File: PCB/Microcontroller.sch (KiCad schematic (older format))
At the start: 36 parts

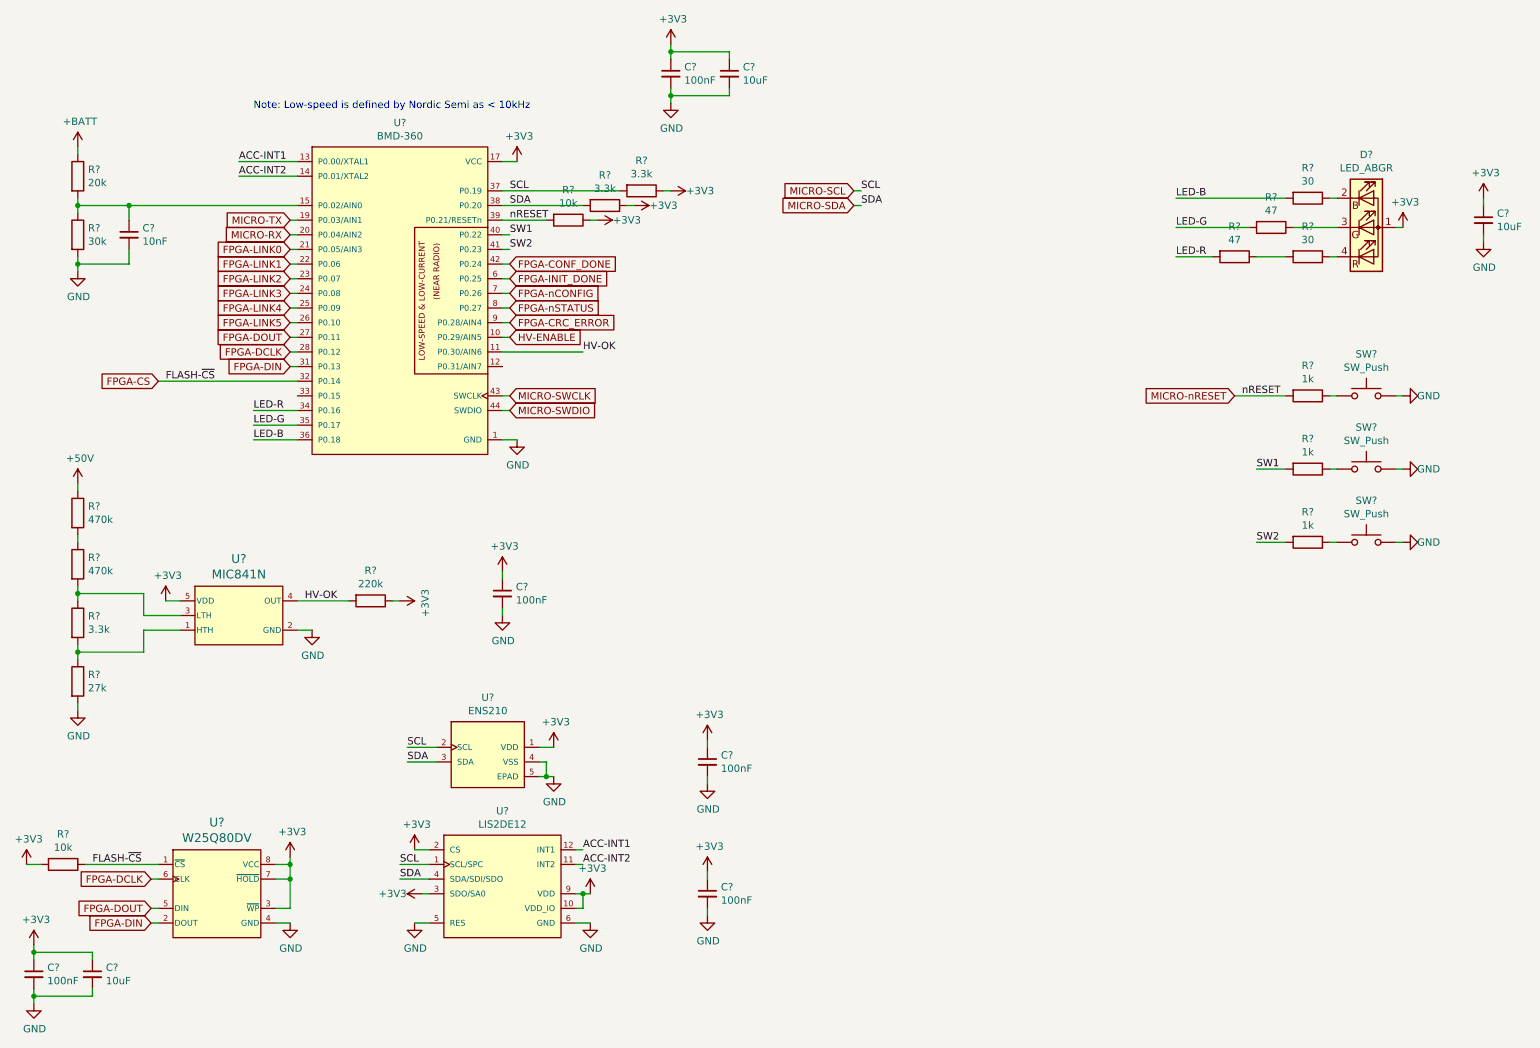
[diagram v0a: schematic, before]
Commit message: Annotate schematic, simplify transmit circuit, shuffle receive opamp stages, reorder buttons so they match net names, reorder connectors to simplify routing, begin arranging parts on PCB
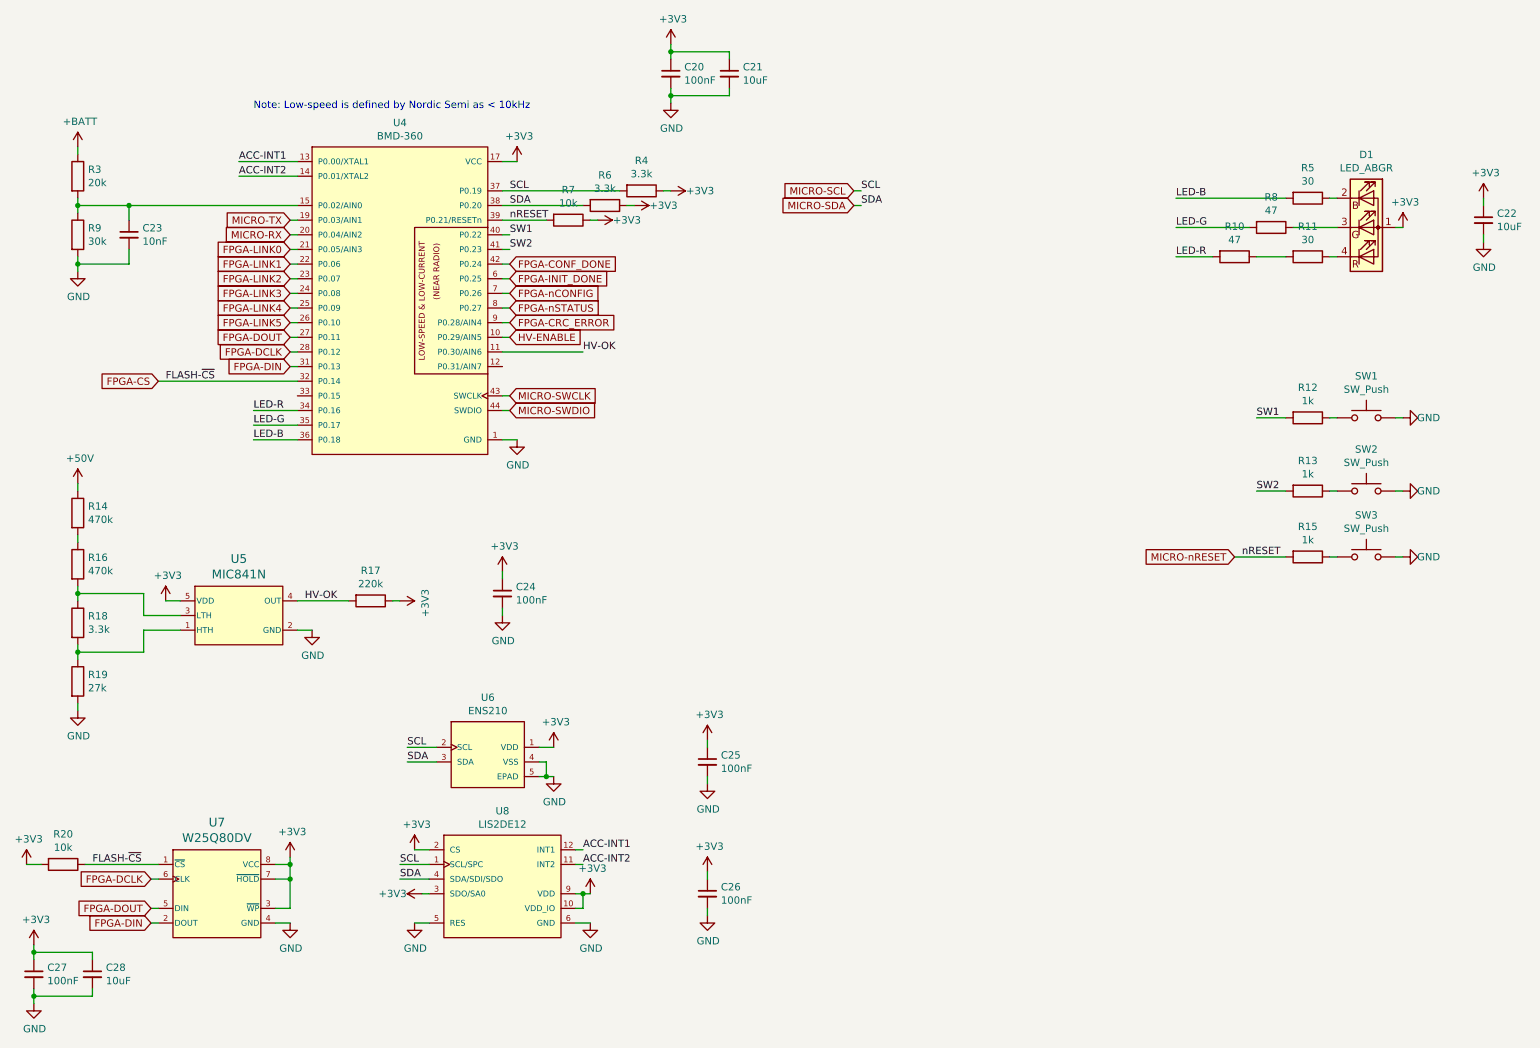
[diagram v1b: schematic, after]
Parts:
- gave numbers to parts that had none: 36
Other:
- moved on the sheet: R12, R13, R15, SW1, SW2, SW3

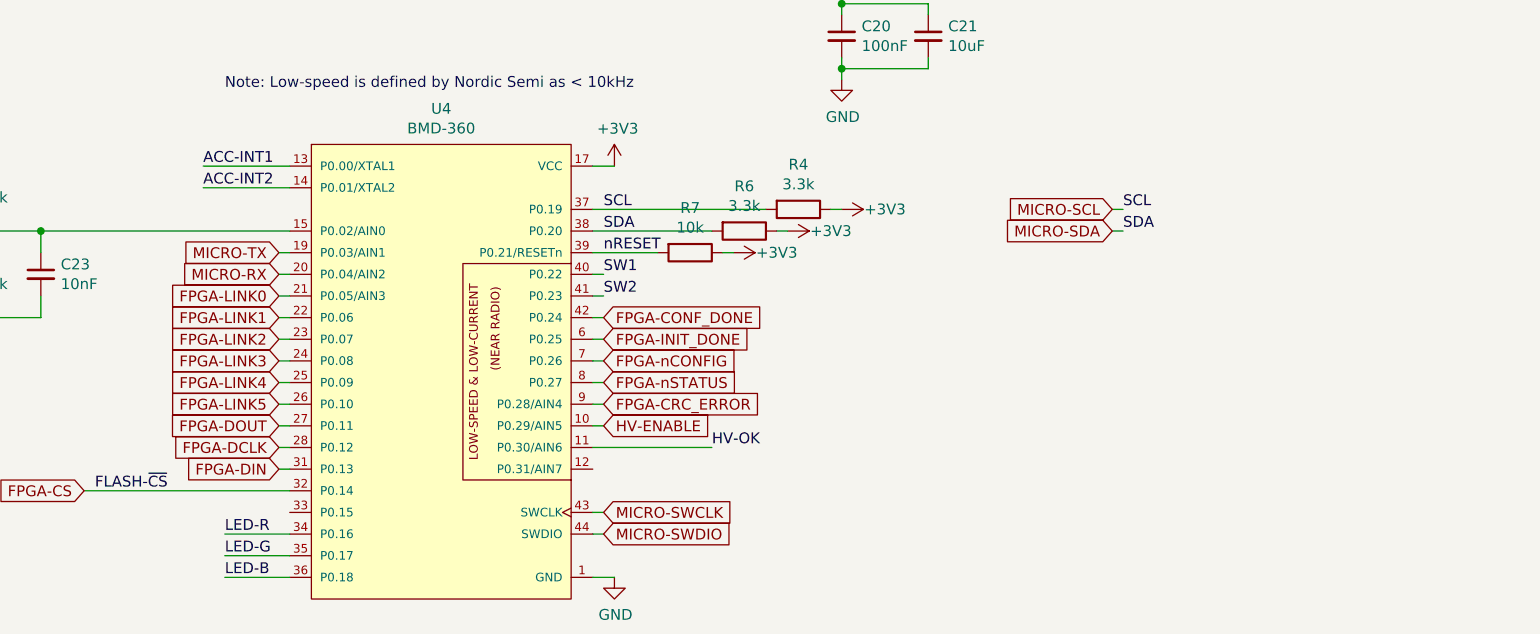
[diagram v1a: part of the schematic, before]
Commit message: Begin layout around FPGA and microcontroller, rearrange some connections to FPGA and microcontroller, change groupings of optional debug pins
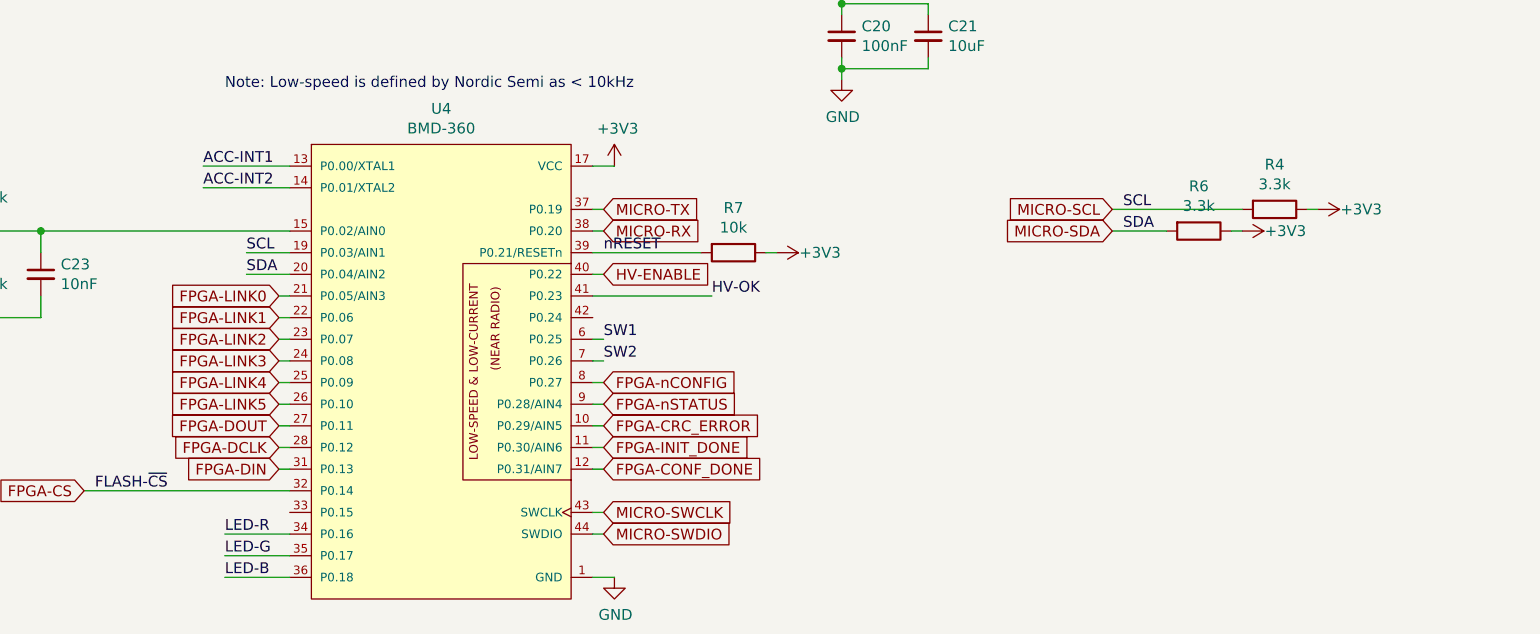
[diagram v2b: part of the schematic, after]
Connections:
- net FPGA-CONF_DONE: now also U4.12 (P0.31/AIN7); no longer U4.42 (P0.24)
- net FPGA-CRC_ERROR: now also U4.10 (P0.29/AIN5); no longer U4.9 (P0.28/AIN4)
- net FPGA-INIT_DONE: now also U4.11 (P0.30/AIN6); no longer U4.6 (P0.25)
- net FPGA-nCONFIG: now also U4.8 (P0.27); no longer U4.7 (P0.26)
- net FPGA-nSTATUS: now also U4.9 (P0.28/AIN4); no longer U4.8 (P0.27)
- net HV-ENABLE: now also U4.40 (P0.22); no longer U4.10 (P0.29/AIN5)
- net HV-OK: now also U4.41 (P0.23); no longer U4.11 (P0.30/AIN6)
- net MICRO-RX: now also U4.38 (P0.20); no longer U4.20 (P0.04/AIN2)
- net MICRO-SCL: now also U4.19 (P0.03/AIN1); no longer U4.37 (P0.19)
- net MICRO-SDA: now also U4.20 (P0.04/AIN2); no longer U4.38 (P0.20)
- net MICRO-TX: now also U4.37 (P0.19); no longer U4.19 (P0.03/AIN1)
- net SW1: now also U4.6 (P0.25); no longer U4.40 (P0.22)
- net SW2: now also U4.7 (P0.26); no longer U4.41 (P0.23)
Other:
- moved on the sheet: R4, R6, R7
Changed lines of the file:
@@
 	1    0    0    -1
 $EndComp
-Text GLabel 2500 2100 0    50   Input ~ 0
+Text GLabel 4000 1900 2    50   Input ~ 0
 MICRO-TX
-Text GLabel 2500 2200 0    50   Input ~ 0
+Text GLabel 4000 2000 2    50   Input ~ 0
 MICRO-RX
 Text GLabel 8950 4400 0    50   Input ~ 0
 MICRO-nRESET
-Text GLabel 4000 2700 2    50   Input ~ 0
+Text GLabel 4000 2800 2    50   Input ~ 0
 FPGA-nSTATUS
 Text GLabel 2500 3000 0    50   Input ~ 0
@@
 Text GLabel 2500 3100 0    50   Input ~ 0
 FPGA-DIN
-Text GLabel 4000 2600 2    50   Input ~ 0
+Text GLabel 4000 2700 2    50   Input ~ 0
 FPGA-nCONFIG
-Text GLabel 4000 2400 2    50   Input ~ 0
+Text GLabel 4000 3100 2    50   Input ~ 0
 FPGA-CONF_DONE
-Text GLabel 4000 2500 2    50   Input ~ 0
+Text GLabel 4000 3000 2    50   Input ~ 0
 FPGA-INIT_DONE
-Text GLabel 4000 2800 2    50   Input ~ 0
+Text GLabel 4000 2900 2    50   Input ~ 0
 FPGA-CRC_ERROR
-Text Label 4000 1900 0    50   ~ 0
+Text Label 2350 2100 0    50   ~ 0
 SCL
-Text Label 4000 2000 0    50   ~ 0
+Text Label 2350 2200 0    50   ~ 0
 SDA
 Wire Wire Line
@@
 	9300 2350 9100 2350
 Wire Wire Line
-	3950 2400 4000 2400
-Wire Wire Line
 	3950 2200 4000 2200
 Wire Wire Line
-	3950 2300 4000 2300
+	3950 2300 4500 2300
 Text Label 2250 3400 0    50   ~ 0
 LED-R
@@
 nRESET
 Wire Wire Line
-	3950 2100 4250 2100
+	3950 2100 4450 2100
 $Comp
 L Device:R R7
 U 1 1 5DFF7E66
-P 4400 2100
-F 0 "R7" V 4193 2100 50  0000 C CNN
-F 1 "10k" V 4284 2100 50  0000 C CNN
-F 2 "Resistors_SMD:R_0603_HandSoldering" V 4330 2100 50  0001 C CNN
-F 3 "https://www.digikey.ca/product-detail/en/stackpole-electronics-inc/RMCF0603FT10K0/RMCF0603FT10K0CT-ND/1943057" H 4400 2100 50  0001 C CNN
-	1    4400 2100
+P 4600 2100
+F 0 "R7" V 4393 2100 50  0000 C CNN
+F 1 "10k" V 4484 2100 50  0000 C CNN
+F 2 "Resistors_SMD:R_0603_HandSoldering" V 4530 2100 50  0001 C CNN
+F 3 "https://www.digikey.ca/product-detail/en/stackpole-electronics-inc/RMCF0603FT10K0/RMCF0603FT10K0CT-ND/1943057" H 4600 2100 50  0001 C CNN
+	1    4600 2100
 	0    1    1    0
 $EndComp
@@
 L power:+3V3 #PWR035
 U 1 1 5DFFAB56
-P 4600 2100
-F 0 "#PWR035" H 4600 1950 50  0001 C CNN
-F 1 "+3V3" V 4600 2300 50  0000 C CNN
-F 2 "" H 4600 2100 50  0001 C CNN
-F 3 "" H 4600 2100 50  0001 C CNN
-	1    4600 2100
-	0    1    1    0
-$EndComp
-Wire Wire Line
-	4550 2100 4600 2100
+P 4800 2100
+F 0 "#PWR035" H 4800 1950 50  0001 C CNN
+F 1 "+3V3" V 4800 2300 50  0000 C CNN
+F 2 "" H 4800 2100 50  0001 C CNN
+F 3 "" H 4800 2100 50  0001 C CNN
+	1    4800 2100
+	0    1    1    0
+$EndComp
+Wire Wire Line
+	4750 2100 4800 2100
 Text Label 9000 4400 0    50   ~ 0
 nRESET
@@
 Wire Wire Line
 	10050 3950 10100 3950
-Text Label 4000 2200 0    50   ~ 0
+Text Label 4000 2500 0    50   ~ 0
 SW1
-Text Label 4000 2300 0    50   ~ 0
+Text Label 4000 2600 0    50   ~ 0
 SW2
 Wire Wire Line
@@
 L Device:R R6
 U 1 1 5E02C855
-P 4650 2000
-F 0 "R6" V 4443 2000 50  0000 C CNN
-F 1 "3.3k" V 4534 2000 50  0000 C CNN
-F 2 "Resistors_SMD:R_0603_HandSoldering" V 4580 2000 50  0001 C CNN
-F 3 "https://www.digikey.ca/product-detail/en/stackpole-electronics-inc/RMCF0603FT3K30/RMCF0603FT3K30CT-ND/1943024" H 4650 2000 50  0001 C CNN
-	1    4650 2000
+P 6750 2000
+F 0 "R6" V 6543 2000 50  0000 C CNN
+F 1 "3.3k" V 6634 2000 50  0000 C CNN
+F 2 "Resistors_SMD:R_0603_HandSoldering" V 6680 2000 50  0001 C CNN
+F 3 "https://www.digikey.ca/product-detail/en/stackpole-electronics-inc/RMCF0603FT3K30/RMCF0603FT3K30CT-ND/1943024" H 6750 2000 50  0001 C CNN
+	1    6750 2000
 	0    1    1    0
 $EndComp
@@
 L Device:R R4
 U 1 1 5E033214
-P 4900 1900
-F 0 "R4" V 4693 1900 50  0000 C CNN
-F 1 "3.3k" V 4784 1900 50  0000 C CNN
-F 2 "Resistors_SMD:R_0603_HandSoldering" V 4830 1900 50  0001 C CNN
-F 3 "https://www.digikey.ca/product-detail/en/stackpole-electronics-inc/RMCF0603FT3K30/RMCF0603FT3K30CT-ND/1943024" H 4900 1900 50  0001 C CNN
-	1    4900 1900
-	0    1    1    0
-$EndComp
-Wire Wire Line
-	3950 2000 4500 2000
-Wire Wire Line
-	3950 1900 4750 1900
+P 7100 1900
+F 0 "R4" V 6893 1900 50  0000 C CNN
+F 1 "3.3k" V 6984 1900 50  0000 C CNN
+F 2 "Resistors_SMD:R_0603_HandSoldering" V 7030 1900 50  0001 C CNN
+F 3 "https://www.digikey.ca/product-detail/en/stackpole-electronics-inc/RMCF0603FT3K30/RMCF0603FT3K30CT-ND/1943024" H 7100 1900 50  0001 C CNN
+	1    7100 1900
+	0    1    1    0
+$EndComp
 $Comp
 L power:+3V3 #PWR034
 U 1 1 5E03E227
-P 4850 2000
-F 0 "#PWR034" H 4850 1850 50  0001 C CNN
-F 1 "+3V3" V 4850 2200 50  0000 C CNN
-F 2 "" H 4850 2000 50  0001 C CNN
-F 3 "" H 4850 2000 50  0001 C CNN
-	1    4850 2000
+P 6950 2000
+F 0 "#PWR034" H 6950 1850 50  0001 C CNN
+F 1 "+3V3" V 6950 2200 50  0000 C CNN
+F 2 "" H 6950 2000 50  0001 C CNN
+F 3 "" H 6950 2000 50  0001 C CNN
+	1    6950 2000
 	0    1    1    0
 $EndComp
@@
 L power:+3V3 #PWR032
 U 1 1 5E03E918
-P 5100 1900
-F 0 "#PWR032" H 5100 1750 50  0001 C CNN
-F 1 "+3V3" V 5100 2100 50  0000 C CNN
-F 2 "" H 5100 1900 50  0001 C CNN
-F 3 "" H 5100 1900 50  0001 C CNN
-	1    5100 1900
-	0    1    1    0
-$EndComp
-Wire Wire Line
-	5050 1900 5100 1900
-Wire Wire Line
-	4800 2000 4850 2000
+P 7300 1900
+F 0 "#PWR032" H 7300 1750 50  0001 C CNN
+F 1 "+3V3" V 7300 2100 50  0000 C CNN
+F 2 "" H 7300 1900 50  0001 C CNN
+F 3 "" H 7300 1900 50  0001 C CNN
+	1    7300 1900
+	0    1    1    0
+$EndComp
+Wire Wire Line
+	7250 1900 7300 1900
+Wire Wire Line
+	6900 2000 6950 2000
 Text Label 9100 3450 0    50   ~ 0
 SW1
@@
 Wire Wire Line
 	5100 1250 5100 1300
-Wire Wire Line
-	2500 2200 2550 2200
 $Comp
 L power:+BATT #PWR030
@@
 Wire Wire Line
 	10650 2200 10650 2250
-Text GLabel 4000 2900 2    50   Input ~ 0
+Text GLabel 4000 2200 2    50   Input ~ 0
 HV-ENABLE
 Wire Wire Line
@@
 Text GLabel 1600 3200 0    50   Input ~ 0
 FPGA-CS
-Wire Wire Line
-	3950 3000 4500 3000
-Wire Wire Line
-	4000 2900 3950 2900
 Wire Wire Line
 	3950 2800 4000 2800
@@
 Text Label 2600 4700 0    50   ~ 0
 HV-OK
-Text Label 4500 3000 0    50   ~ 0
+Text Label 4500 2300 0    50   ~ 0
 HV-OK
 $Comp
@@
 $EndComp
 Wire Wire Line
-	2500 2100 2550 2100
-Wire Wire Line
 	2250 3400 2550 3400
 Wire Wire Line
@@
 SDA
 Wire Wire Line
-	6350 1900 6400 1900
-Wire Wire Line
-	6350 2000 6400 2000
+	3950 2900 4000 2900
+Wire Wire Line
+	4000 3000 3950 3000
+Wire Wire Line
+	4000 3100 3950 3100
+Wire Wire Line
+	6350 1900 6950 1900
+Wire Wire Line
+	6350 2000 6600 2000
+Wire Wire Line
+	2350 2100 2550 2100
+Wire Wire Line
+	2350 2200 2550 2200
+Wire Wire Line
+	3950 1900 4000 1900
+Wire Wire Line
+	4000 2000 3950 2000
 $EndSCHEMATC

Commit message: Remove unnecessary series resistors, rearrange connections on FPGA and microcontroller, rearrange debug pins, layout most of FPGA and microcontroller sections
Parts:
- removed R12, R13, R15: 1k, Resistors_SMD:R_0603_HandSoldering, symbol Device:R
- renumbered R14 to R12, R16 to R13, R17 to R14, R18 to R15, R19 to R16, R20 to R17
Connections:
- net ACC-INT1: now also U4.19 (P0.03/AIN1); no longer U4.13 (P0.00/XTAL1)
- net FPGA-CONF_DONE: now also U4.10 (P0.29/AIN5); no longer U4.12 (P0.31/AIN7)
- net FPGA-CRC_ERROR: now also U4.12 (P0.31/AIN7); no longer U4.10 (P0.29/AIN5)
- net FPGA-CS: now also U4.24 (P0.08); no longer U4.32 (P0.14)
- net FPGA-DCLK: now also U4.22 (P0.06); no longer U4.28 (P0.12)
- net FPGA-DIN: now also U4.21 (P0.05/AIN3); no longer U4.31 (P0.13)
- net FPGA-DOUT: now also U4.23 (P0.07); no longer U4.27 (P0.11)
- net FPGA-LINK0: now also U4.32 (P0.14); no longer U4.21 (P0.05/AIN3)
- net FPGA-LINK1: now also U4.31 (P0.13); no longer U4.22 (P0.06)
- net FPGA-LINK2: now also U4.28 (P0.12); no longer U4.23 (P0.07)
- net FPGA-LINK3: now also U4.27 (P0.11); no longer U4.24 (P0.08)
- net FPGA-LINK4: now also U4.26 (P0.10); no longer U4.25 (P0.09)
- net FPGA-LINK5: now also U4.25 (P0.09); no longer U4.26 (P0.10)
- net LED-B: now also U4.34 (P0.16); no longer U4.36 (P0.18)
- net LED-R: now also U4.36 (P0.18); no longer U4.34 (P0.16)
- net MICRO-SCL: now also U4.13 (P0.00/XTAL1); no longer U4.19 (P0.03/AIN1)
- net MICRO-SDA: now also U4.15 (P0.02/AIN0); no longer U4.20 (P0.04/AIN2)
- net MICRO-nRESET: now also SW3.1
- net SW1: now also SW1.1
- net SW2: now also SW2.1
- net at C23.1, R3.2, R9.1: now also U4.20 (P0.04/AIN2); no longer U4.15 (P0.02/AIN0)
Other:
- moved on the sheet: C23, R3, R9
